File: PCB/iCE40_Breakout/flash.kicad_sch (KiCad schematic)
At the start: 44 parts, among them J4 prog_hdr, Q10 L2N7002SLLT1G, Q11 L2N7002SLLT1G, Q12 L2N7002SLLT1G, Q2 L2N7002SLLT1G, Q3 L2N7002SLLT1G, Q4 L2N7002SLLT1G, Q5 L2N7002SLLT1G, Q6 L2N7002SLLT1G, Q7 L2N7002SLLT1G, Q8 L2N7002SLLT1G, Q9 L2N7002SLLT1G, U6 W25Q128JVS

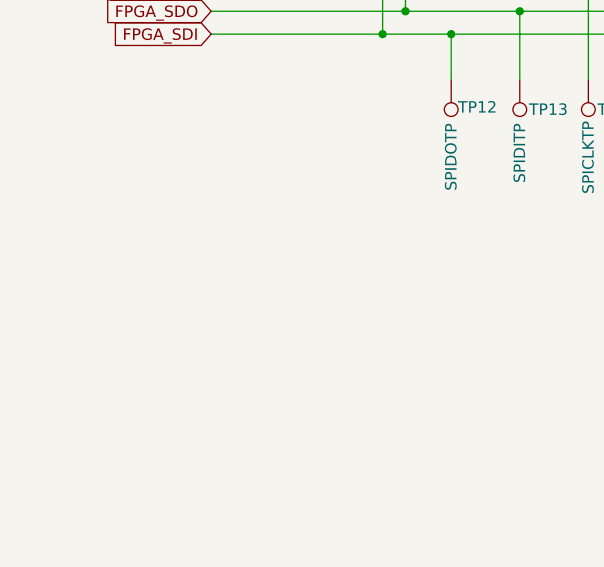
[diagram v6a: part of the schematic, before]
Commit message: Updated all TPs to use pads, not holes for hooks. Also removed duplicate SPI programming TPs
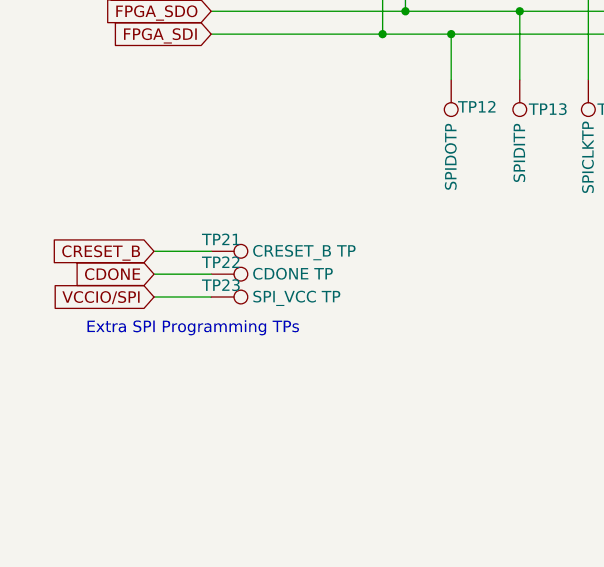
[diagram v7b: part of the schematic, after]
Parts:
- added TP21: CRESET_B TP, TestPoint:TestPoint_Pad_D1.0mm, symbol Connector:TestPoint
- added TP22: CDONE TP, TestPoint:TestPoint_Pad_D1.0mm, symbol Connector:TestPoint
- added TP23: SPI_VCC TP, TestPoint:TestPoint_Pad_D1.0mm, symbol Connector:TestPoint
- TP12, TP13, TP14, TP15: footprint TestPoint:TestPoint_Loop_D1.80mm_Drill1.0mm_Beaded -> TestPoint:TestPoint_Pad_D1.0mm
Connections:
- net CDONE: now also TP22.1
- net CRESET_B: now also TP21.1
- net VCCIO/SPI: now also TP23.1
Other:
- note added: "Extra SPI Programming TPs"

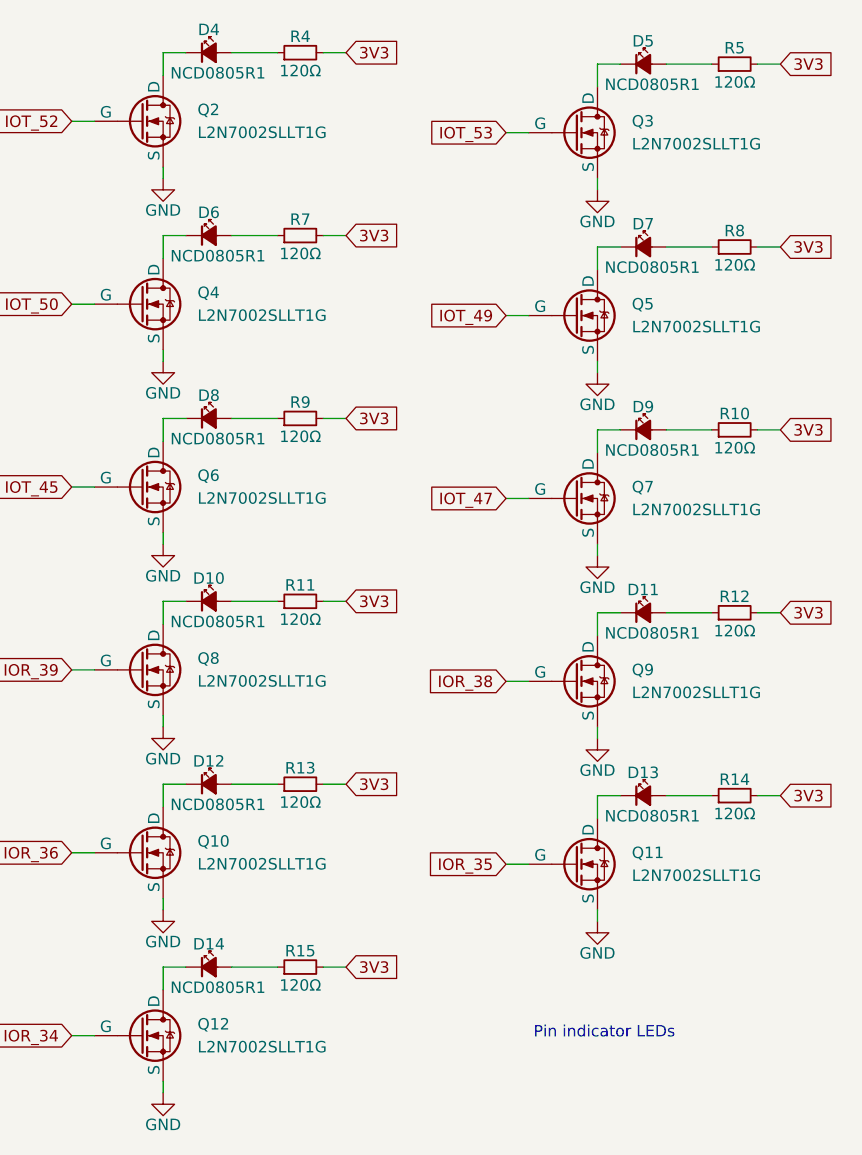
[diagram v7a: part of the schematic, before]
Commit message: Swapped LED and resistor order placement
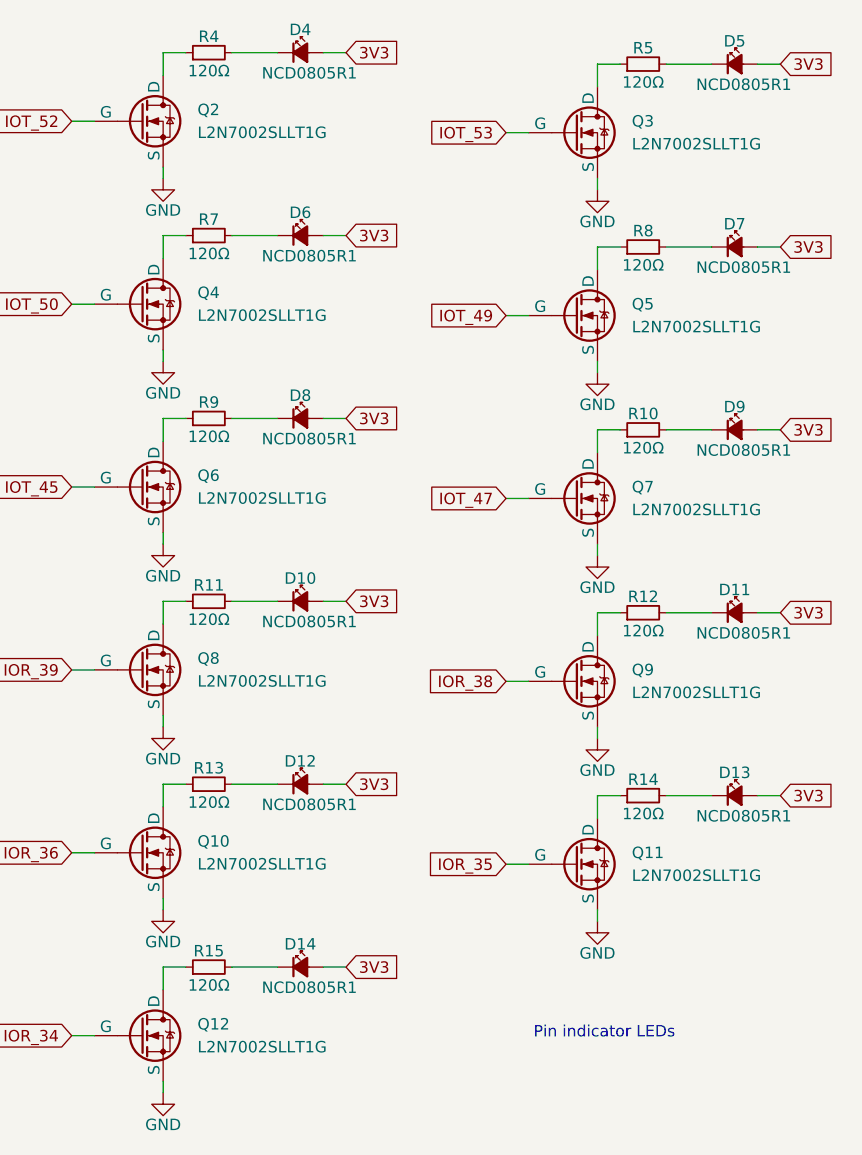
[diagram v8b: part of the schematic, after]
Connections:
- net 3V3: now also D10.2 (A), D11.2 (A), D12.2 (A), D13.2 (A), D14.2 (A), D4.2 (A), D5.2 (A), D6.2 (A), D7.2 (A), D8.2 (A), D9.2 (A); no longer R10.2, R11.2, R12.2, R13.2, R14.2, R15.2, R4.2, R5.2, R7.2, R8.2, R9.2
- net at Q12.1 (D): now also R15.1; no longer D14.1 (K)
- net at Q7.1 (D): now also R10.1; no longer D9.1 (K)
- net at R5.1: now also Q3.1 (D); no longer D5.2 (A)
- net at Q6.1 (D): now also R9.1; no longer D8.1 (K)
- net at Q9.1 (D): now also R12.1; no longer D11.1 (K)
- net at D4.1 (K): now also R4.2; no longer Q2.1 (D)
- net at R4.1: now also Q2.1 (D); no longer D4.2 (A)
- net at R13.1: now also Q10.1 (D); no longer D12.2 (A)
- net at D6.1 (K): now also R7.2; no longer Q4.1 (D)
- net at R7.1: now also Q4.1 (D); no longer D6.2 (A)
- net at D5.1 (K): now also R5.2; no longer Q3.1 (D)
- net at D13.1 (K): now also R14.2; no longer Q11.1 (D)
- net at R14.1: now also Q11.1 (D); no longer D13.2 (A)
- net at D12.1 (K): now also R13.2; no longer Q10.1 (D)
- net at D10.1 (K): now also R11.2; no longer Q8.1 (D)
- net at R11.1: now also Q8.1 (D); no longer D10.2 (A)
- net at Q5.1 (D): now also R8.1; no longer D7.1 (K)
- new net: D14.1 (K), R15.2
- new net: D9.1 (K), R10.2
- new net: D11.1 (K), R12.2
- new net: D8.1 (K), R9.2
- new net: D7.1 (K), R8.2
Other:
- moved on the sheet: D10, D11, D12, D13, D14, D4, D5, D6, D7, D8, D9, R10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
